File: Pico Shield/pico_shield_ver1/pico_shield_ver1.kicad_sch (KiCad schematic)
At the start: 1 part

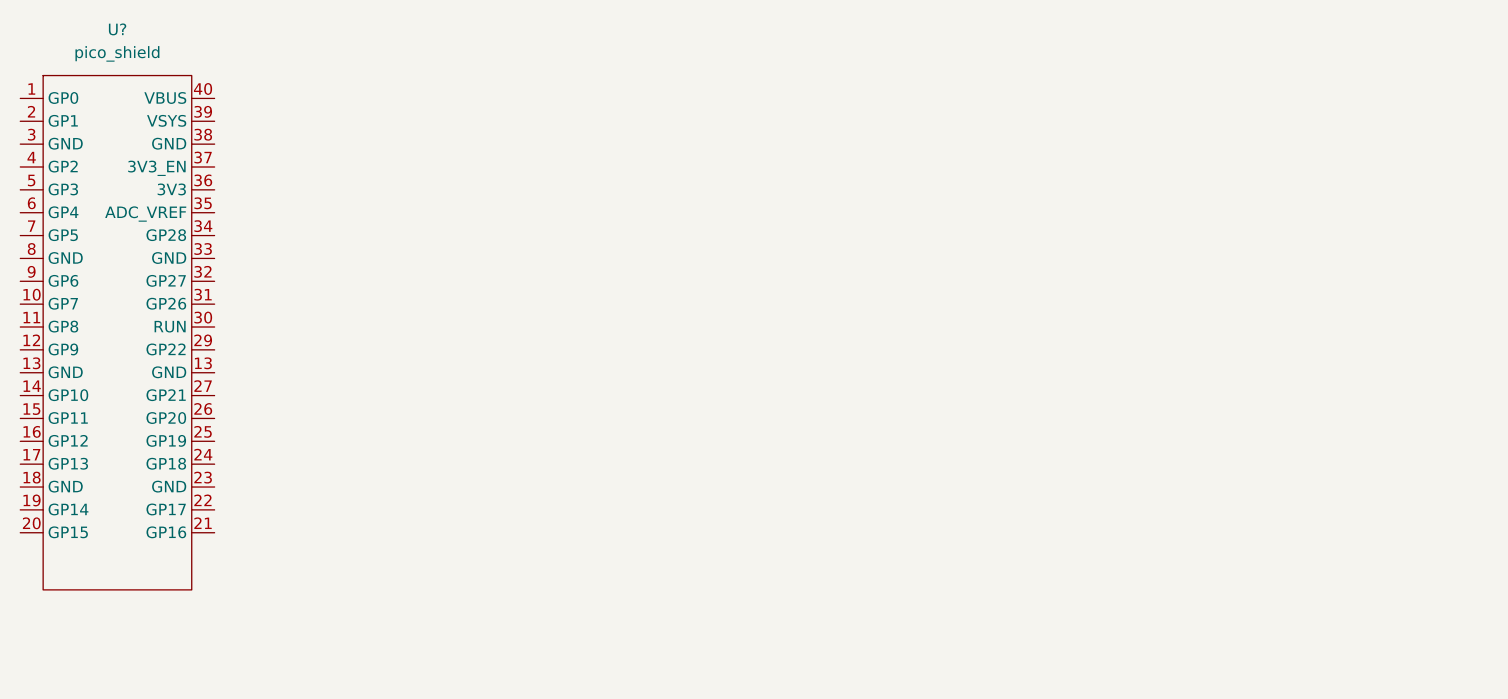
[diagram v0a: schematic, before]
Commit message: Stepper Driver Implemented
Found schematic for stepper motor driver board. Added the model to the current pico shield schematic.
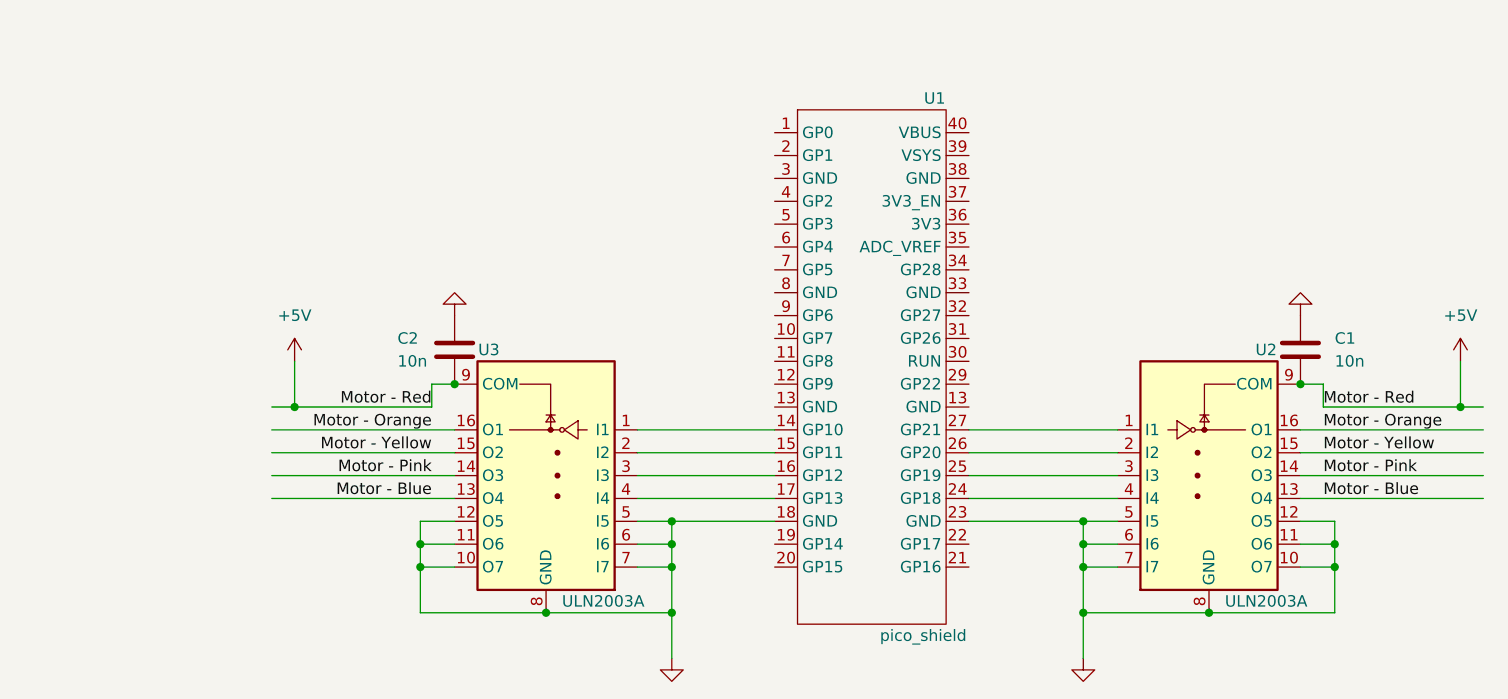
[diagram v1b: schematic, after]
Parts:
- added C1, C2: 10n, symbol Device:C
- added U2, U3: ULN2003A, symbol Transistor_Array:ULN2003A
- gave numbers to parts that had none: 1
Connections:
- net at U1.14 (GP10): now also U3.1 (I1)
- net at U1.15 (GP11): now also U3.2 (I2)
- net at U1.16 (GP12): now also U3.3 (I3)
- net at U1.17 (GP13): now also U3.4 (I4)
- net GND: now reaches U1.18 (GND)
- net GND: now also U1.23 (GND), C1.1, C2.1, U2.10 (O7), U2.11 (O6), U2.12 (O5), U2.5 (I5), U2.6 (I6), U2.7 (I7), U2.8 (GND), U3.10 (O7), U3.11 (O6), U3.12 (O5), U3.5 (I5), U3.6 (I6), U3.7 (I7), U3.8 (GND)
- net at U1.24 (GP18): now also U2.4 (I4)
- net at U1.25 (GP19): now also U2.3 (I3)
- net at U1.26 (GP20): now also U2.2 (I2)
- net at U1.27 (GP21): now also U2.1 (I1)
- new net +5V: C1.2, C2.2, U2.9 (COM), U3.9 (COM)
- new net Motor - Blue: U2.13 (O4), U3.13 (O4)
- new net Motor - Orange: U2.16 (O1), U3.16 (O1)
- new net Motor - Pink: U2.14 (O3), U3.14 (O3)
- new net Motor - Yellow: U2.15 (O2), U3.15 (O2)
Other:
- moved on the sheet: U1
